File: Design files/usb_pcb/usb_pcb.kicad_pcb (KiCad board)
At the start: 2 copper layers, 36 parts, among them J1 Screw_Terminal_01x02, J2 Conn_01x04_Male, J3 Screw_Terminal_01x02, J4 Screw_Terminal_01x02, J5 Screw_Terminal_01x02, J6 Screw_Terminal_01x02, J7 Screw_Terminal_01x02, SW1 SW_SPST, U1 MCP6024-I/P, U2 NE555, U3 4N35, U4 MCP6021-I/P, U5 L78L05_TO92

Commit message: Created pcb layout and output files
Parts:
- removed C2: 1u, Capacitor_THT:C_Disc_D4.3mm_W1.9mm_P5.00mm
- removed C5: 100n, Capacitor_THT:C_Disc_D4.3mm_W1.9mm_P5.00mm
- removed D1: GREEN LED, LED_THT:LED_D5.0mm
- removed J1, J3, J4, J5, J6, J7: Screw_Terminal_01x02, TerminalBlock_TE-Connectivity:TerminalBlock_TE_282834-2_1x02_P2.54mm_Horizontal
- removed J2: Conn_01x04_Male, Connector_PinHeader_2.54mm:PinHeader_2x02_P2.54mm_Vertical
- removed SW1: SW_SPST, Button_Switch_THT:SW_PUSH_6mm_H5mm
- added P1: Conn_01x02_Male, Connector_PinHeader_2.54mm:PinHeader_1x02_P2.54mm_Vertical, F.Cu at (55.0, 72.5)
- added P10: Conn_01x02_Male, Connector_PinHeader_2.54mm:PinHeader_1x02_P2.54mm_Vertical, F.Cu at (110.0, 50.0)
- added P2: Conn_01x02_Male, Connector_PinHeader_2.54mm:PinHeader_1x02_P2.54mm_Vertical, F.Cu at (82.5, 62.5)
- added P3: Conn_01x05_Male, Connector_PinHeader_2.54mm:PinHeader_1x04_P2.54mm_Vertical, F.Cu at (90.0, 80.0)
- added P4: Conn_01x02_Male, Connector_PinHeader_2.54mm:PinHeader_1x02_P2.54mm_Vertical, F.Cu at (97.5, 87.5)
- added P5: Conn_01x02_Male, Connector_PinHeader_2.54mm:PinHeader_1x02_P2.54mm_Vertical, F.Cu at (142.5, 102.5)
- added P6: Conn_01x08_Male, Connector_PinHeader_2.54mm:PinHeader_1x08_P2.54mm_Vertical, F.Cu at (114.8, 100.0)
- added P7: Conn_01x08_Male, Connector_PinHeader_2.54mm:PinHeader_1x08_P2.54mm_Vertical, F.Cu at (170.0, 92.7)
- added P8: Conn_01x02_Male, Connector_PinHeader_2.54mm:PinHeader_1x02_P2.54mm_Vertical, F.Cu at (100.0, 50.0)
- added P9: Conn_01x02_Male, Connector_PinHeader_2.54mm:PinHeader_1x02_P2.54mm_Vertical, F.Cu at (100.0, 57.5)
- added R6: 220R, Resistor_THT:R_Axial_DIN0204_L3.6mm_D1.6mm_P7.62mm_Horizontal, F.Cu at (115.0, 57.5)
- H1, H3: footprint MountingHole:MountingHole_3.2mm_M3 -> MountingHole:MountingHole_3.2mm_M3_Pad_Via
- H2, H4: value MountingHole -> MountingHole_Pad; footprint MountingHole:MountingHole_3.2mm_M3 -> MountingHole:MountingHole_3.2mm_M3_Pad_Via
- moved H1 149.3 mm to (57.5, 50.0)
- moved H2 123.5 mm to (167.5, 50.0)
- moved H3 120.7 mm to (57.5, 102.5)
- moved R5 116.2 mm to (157.5, 67.5)
- moved R4 109.5 mm to (165.0, 62.5), turned to 180 degrees
- moved C8 82.2 mm to (100.0, 62.5), turned to 0 degrees
- moved H4 72.9 mm to (167.5, 100.0)
- moved U5 67.1 mm to (107.5, 70.0), turned to 180 degrees
- moved D2 65.1 mm to (62.5, 80.0), turned to 90 degrees
- moved U1 57.9 mm to (152.5, 75.0), turned to 0 degrees
- moved R1 56.1 mm to (67.5, 80.0), turned to 90 degrees
- moved C6 54.5 mm to (112.5, 70.0), turned to 90 degrees
- moved U3 53.5 mm to (75.0, 72.5), turned to 0 degrees
- moved C7 48.3 mm to (117.5, 70.0), turned to 90 degrees
- moved C3 48.2 mm to (145.0, 77.5), turned to 270 degrees
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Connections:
- H2 pad 1: (no net) -> GND
- H4 pad 1: (no net) -> GND
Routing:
- net GND: track 0.00 -> 316.4 mm
- net +5V: track 0.00 -> 169.3 mm
- net /OUT_PULSE: track 0.00 -> 70.3 mm
- net Net-(P2-Pad1): track 0.00 -> 38.7 mm
- net Net-(C3-Pad1): track 0.00 -> 37.0 mm
- net Net-(P3-Pad1): track 0.00 -> 24.6 mm
- net Net-(C8-Pad1): track 0.00 -> 23.5 mm
- net Net-(P7-Pad2): track 0.00 -> 22.8 mm
- net Net-(C4-Pad1): track 0.00 -> 20.9 mm
- net Net-(P1-Pad2): track 0.00 -> 20.0 mm
- net Net-(R4-Pad2): track 0.00 -> 18.7 mm
- net Net-(P7-Pad8): track 0.00 -> 15.7 mm
- net Net-(P7-Pad4): track 0.00 -> 15.3 mm
- net Net-(P7-Pad6): track 0.00 -> 13.9 mm
- net Net-(D2-Pad2): track 0.00 -> 8.60 mm
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- added copper zone on B.Cu, net (none)
- added copper zone on F.Cu, net (none)
- added copper zone on F.Cu, net +5V
- added copper zone on B.Cu, net GND
- added copper zone on F.Cu, net GND
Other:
- board outline added: 120 x 62.5 mm
- net class Default: trace_width 0.25 -> 0.5; via_drill 0.4 -> 0.5
- rule trace_min: 0.2 -> 0.4
- rule via_min_drill: 0.3 -> 0.5
- rule via_min_size: 0.4 -> 0.8

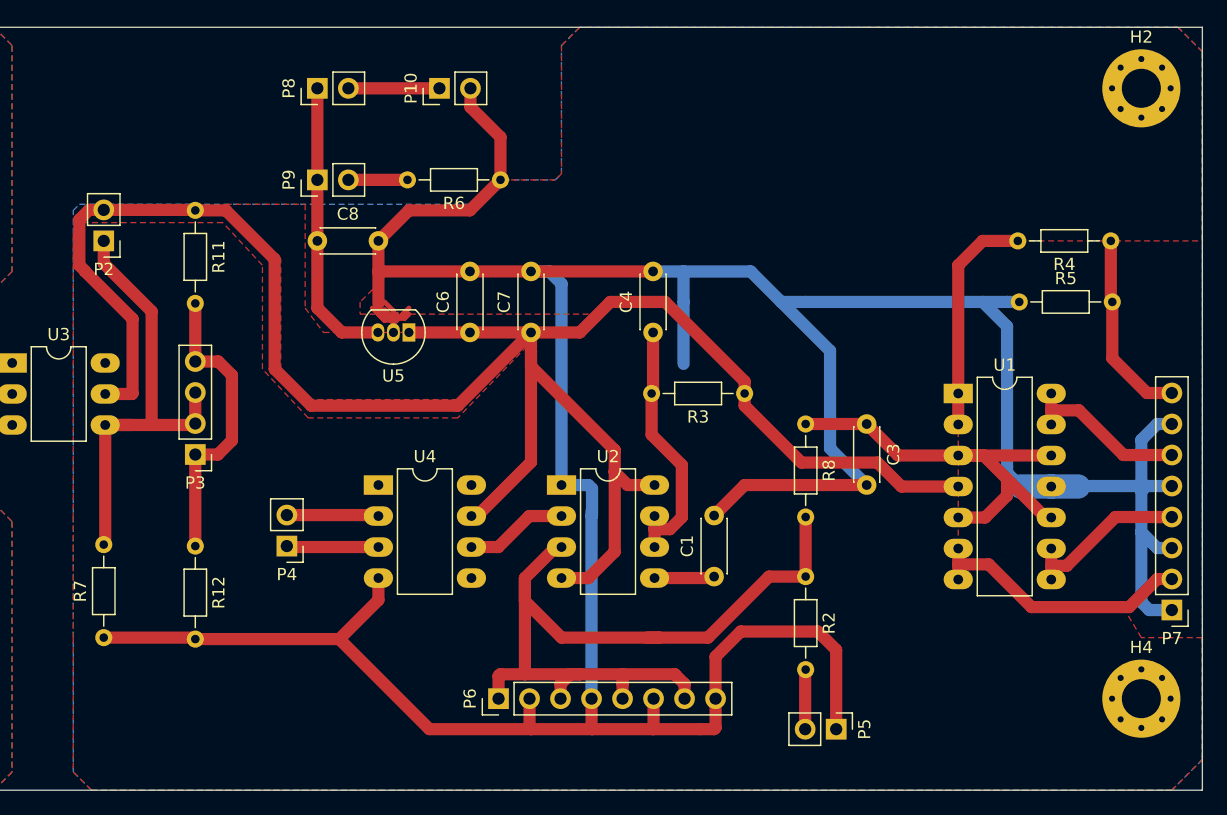
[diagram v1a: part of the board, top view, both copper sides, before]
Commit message: Ground and power planes modified. Manual trigger position modified to work with any polarity setting
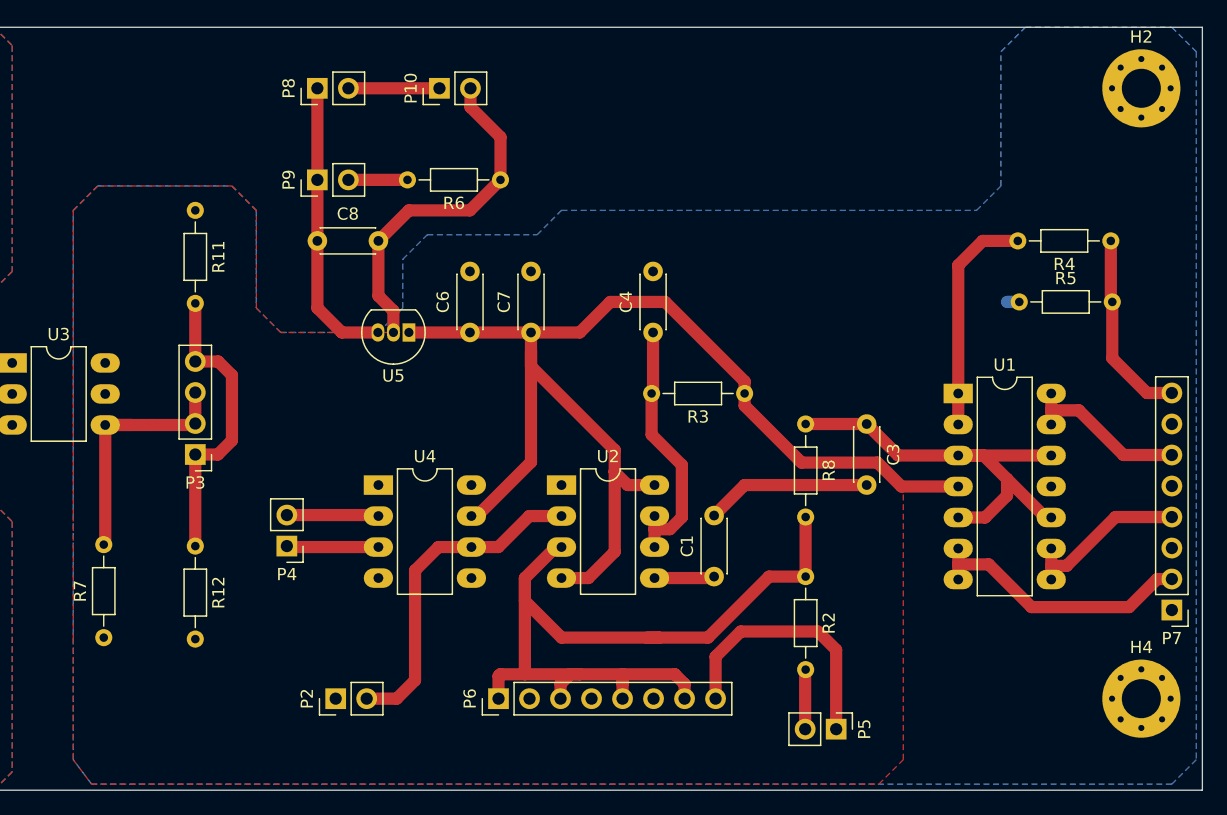
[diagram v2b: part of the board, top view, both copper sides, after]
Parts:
- moved P2 42.0 mm to (101.5, 100.0), turned to 90 degrees
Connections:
- P2 pad 1: Net-(P2-Pad1) -> GND
- P2 pad 2: +5V -> Net-(P2-Pad2)
- P3 pad 2: Net-(P2-Pad1) -> Net-(P3-Pad2)
- P3 pad 3: Net-(P2-Pad1) -> Net-(P3-Pad2)
- R7 pad 2: Net-(P2-Pad1) -> Net-(P3-Pad2)
- U2 pad 2: Net-(U2-Pad2) -> Net-(P2-Pad2)
- U3 pad 4: Net-(P2-Pad1) -> Net-(P3-Pad2)
- U4 pad 6: Net-(U2-Pad2) -> Net-(P2-Pad2)
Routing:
- net GND: track 316.4 -> 64.7 mm
- net +5V: track 169.3 -> 99.3 mm
- net Net-(P2-Pad1): track 38.7 -> 0.00 mm
- net Net-(P2-Pad2): track 0.00 -> 27.4 mm
- net Net-(P3-Pad2): track 0.00 -> 22.0 mm
- net Net-(U2-Pad2): track 8.43 -> 0.00 mm
- removed copper zone on F.Cu, net GND

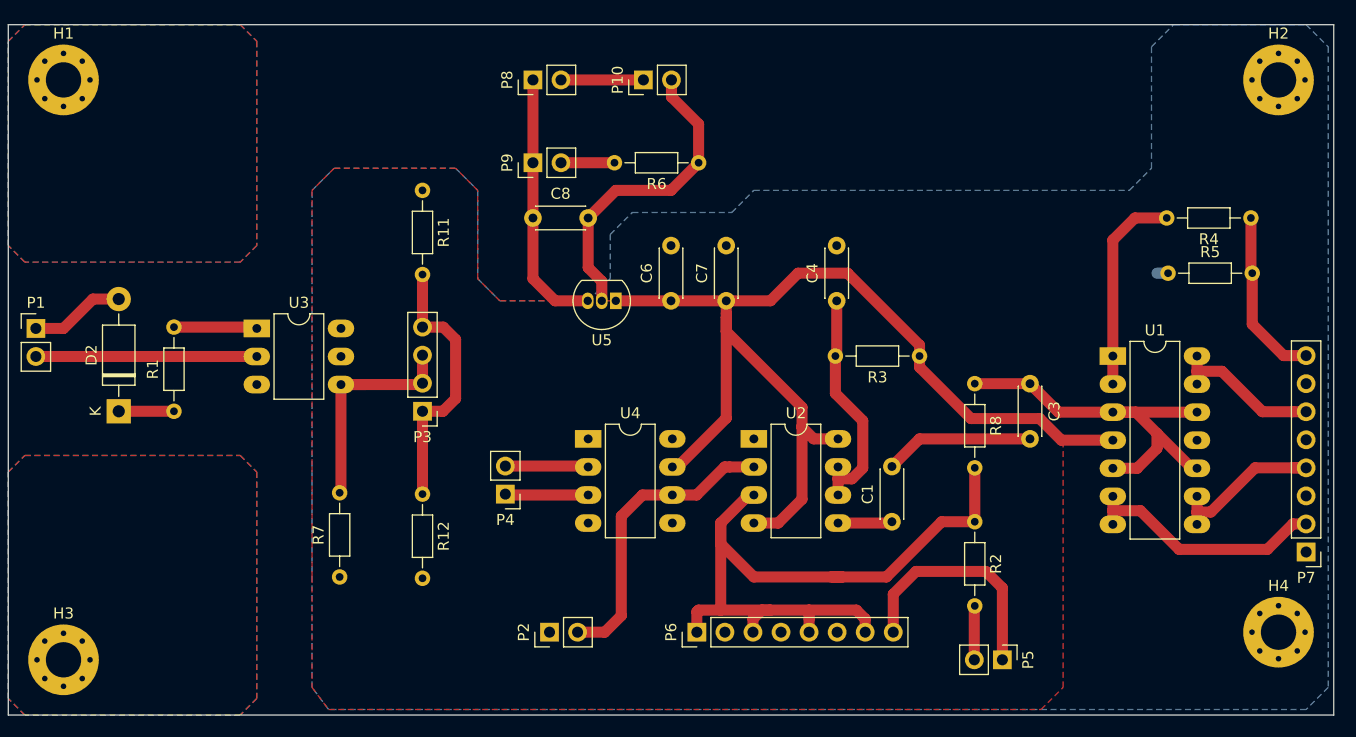
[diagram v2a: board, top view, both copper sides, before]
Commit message: Minor modifications for first production run, gerber updated
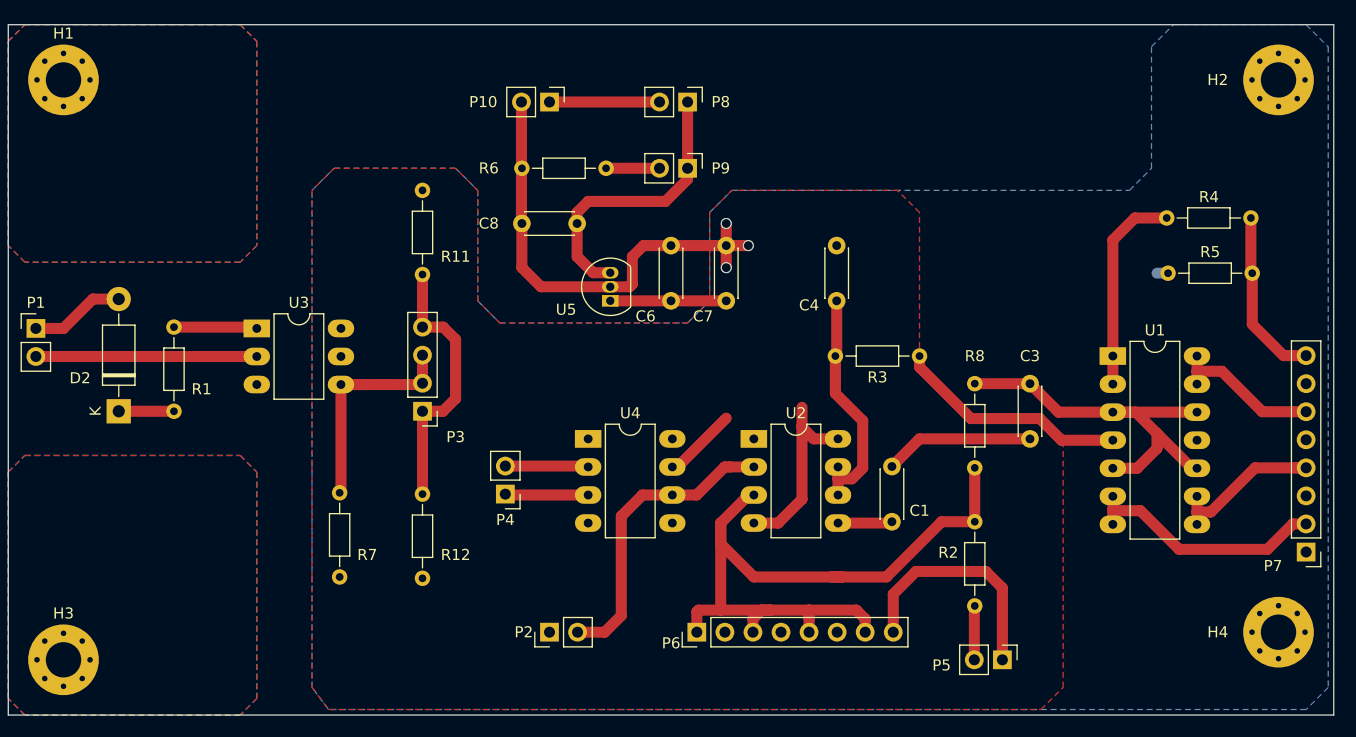
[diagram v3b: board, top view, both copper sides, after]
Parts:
- moved R6 16.0 mm to (99.0, 58.0), turned to 0 degrees
- moved P8 14.1 mm to (114.0, 52.0), turned to 270 degrees
- moved P9 14.0 mm to (114.0, 58.0), turned to 270 degrees
- moved P10 8.73 mm to (101.5, 52.0), turned to 270 degrees
- moved C8 4.03 mm to (104.0, 63.0), turned to 180 degrees
- moved U5 0.50 mm to (107.0, 70.0), turned to 90 degrees
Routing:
- net +5V: track 99.3 -> 56.3 mm
- net GND: track 64.7 -> 79.3 mm, vias 0 -> 3
- net Net-(P10-Pad1): track 7.46 -> 9.96 mm
- net Net-(C8-Pad1): track 23.5 -> 25.8 mm
